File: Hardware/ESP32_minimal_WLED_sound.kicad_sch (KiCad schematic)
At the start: 42 parts, among them J1 Conn_01x04_Male, J2 USB_C_Receptacle_USB2.0, J3 Conn_01x02_Male, Q1 AO3400A, SW1 Reset, SW2 Boot, U1 LM1117-3.3, U2 ESP32-S2-WROVER, U3 USBLC6-2SC6, U4 TXS0102DCT

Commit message: update to V1
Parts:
- removed C3, C4: 20p, Capacitor_SMD:C_0603_1608Metric, symbol Device:C_Small
- removed C5, C9: 0.1u, Capacitor_SMD:C_0603_1608Metric, symbol Device:C_Small
- removed D1: LED, LED_SMD:LED_0603_1608Metric, symbol Device:LED_Small
- removed FB1, FB2: >1A, Inductor_SMD:L_0603_1608Metric, symbol Device:Ferrite_Bead_Small
- removed JP1: SolderJumper_2_Bridged, Jumper:SolderJumper-2_P1.3mm_Bridged_RoundedPad1.0x1.5mm, symbol Jumper:SolderJumper_2_Bridged
- removed JP2: SolderJumper_3_Bridged12, Jumper:SolderJumper-3_P1.3mm_Bridged12_Pad1.0x1.5mm, symbol Jumper:SolderJumper_3_Bridged12
- removed R2: 100r, Resistor_SMD:R_0603_1608Metric, symbol Device:R_Small
- removed R3, R4: 22r, Resistor_SMD:R_0603_1608Metric, symbol Device:R_Small
- removed SW1: Reset, ESP32-S2-Breakout:Alps_SKRK, symbol Switch:SW_Push
- removed U2: ESP32-S2-WROVER, RF_Module:ESP32-S2-WROVER, symbol RF_Module:ESP32-S2-WROVER
- removed U3: USBLC6-2SC6, Package_TO_SOT_SMD:SOT-23-6, symbol Power_Protection:USBLC6-2SC6
- added C3, C4, C9: 0.1uF, Capacitor_SMD:C_0805_2012Metric, symbol Device:C
- added C5: 0.1uF, Capacitor_SMD:C_0603_1608Metric, symbol Device:C
- added J4: Barrel_Jack_Switch_Pin3Ring, Connector_BarrelJack:BarrelJack_GCT_DCJ200-10-A_Horizontal, symbol Connector:Barrel_Jack_Switch_Pin3Ring
- added J5, J6: Conn_01x03_Male, Connector_JST:JST_EH_B3B-EH-A_1x03_P2.50mm_Vertical, symbol Connector:Conn_01x03_Male
- added J7, J9: Conn_01x03_Male, Connector_PinHeader_2.54mm:PinHeader_1x03_P2.54mm_Vertical, symbol Connector:Conn_01x03_Male
- added J8: Conn_01x02_Male, TerminalBlock_Phoenix:TerminalBlock_Phoenix_MKDS-1,5-2-5.08_1x02_P5.08mm_Horizontal, symbol Connector:Conn_01x02_Male
- added JP1: SolderJumper_3_Open, Jumper:SolderJumper-3_P1.3mm_Open_Pad1.0x1.5mm, symbol Jumper:SolderJumper_3_Open
- added MK1: ICS-43434, ICS-43434:MIC_ICS-43434, symbol ICS-43434:ICS-43434
- added R14, R15: 4,7k, Resistor_SMD:R_0603_1608Metric, symbol Device:R
- added R2: 0.01, Resistor_SMD:R_0805_2012Metric, symbol Device:R
- added R3, R4: 10, Resistor_SMD:R_0603_1608Metric, symbol Device:R
- added U2: INA226, Package_SO:VSSOP-10_3x3mm_P0.5mm, symbol Analog_ADC:INA226
- added U3: LM1117-3.3, Package_TO_SOT_SMD:SOT-223, symbol Regulator_Linear:LM1117-3.3
- added U5: ESP32-WROOM-32, RF_Module:ESP32-WROOM-32, symbol RF_Module:ESP32-WROOM-32
- C10, C11: footprint Capacitor_SMD:C_0603_1608Metric_Pad1.08x0.95mm_HandSolder -> Capacitor_SMD:C_0603_1608Metric
- J1: footprint Connector_PinHeader_2.54mm:PinHeader_1x04_P2.54mm_Horizontal -> Connector_PinHeader_2.54mm:PinHeader_1x04_P2.54mm_Vertical
- J2: footprint ESP32-S2-Breakout:USB_C_Receptacle_HRO_TYPE-C-31-M-12 -> Connector_USB:USB_C_Receptacle_HRO_TYPE-C-31-M-12
- J3: footprint Connector_Phoenix_MSTB:PhoenixContact_MSTBA_2,5_2-G-5,08_1x02_P5.08mm_Horizontal -> TerminalBlock_Phoenix:TerminalBlock_Phoenix_MKDS-1,5-2-5.08_1x02_P5.08mm_Horizontal
- R1: value 10k -> 1M; LCSC C99198 -> C163928
- R12, R13: footprint Capacitor_SMD:C_0603_1608Metric_Pad1.08x0.95mm_HandSolder -> Resistor_SMD:R_0603_1608Metric
- R6, R7, R9: footprint Resistor_SMD:R_0805_2012Metric -> Resistor_SMD:R_0603_1608Metric
- R8: value 100r -> 100
- SW2: footprint ESP32-S2-Breakout:Alps_SKRK -> Button_Switch_SMD:SW_SPST_B3U-1000P-B
- U1: value LM1117-3.3 -> LM1117-5
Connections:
- net VBUS is gone; now on net +5V: J2.A4 (VBUS), J2.A9 (VBUS), J2.B4 (VBUS), J2.B9 (VBUS)
- net +12V: now also C5.2, J4.1, J8.1 (Pin_1), R2.2, R3.1; no longer J1.4 (Pin_4)
- net +3V3: now also J1.4 (Pin_4), R8.1, C4.2, C9.1, MK1.5 (VDD), R14.2, R15.1, U2.6 (VS), U3.2 (VO), U5.2 (VDD); no longer C2.2, J1.3 (Pin_3), R1.1, U1.2 (VO)
- net +5V: now also C2.2, U1.2 (VO), C3.1, J5.1 (Pin_1), J6.1 (Pin_1), J7.1 (Pin_1), J9.1 (Pin_1), JP1.1 (A), U3.3 (VI); no longer C1.1, U1.3 (VI)
- net EN: now also C7.2, U5.3 (EN)
- net GND: now also R1.2, C3.2, C4.1, C9.2, J4.2, J4.3, J5.3 (Pin_3), J6.3 (Pin_3), J7.3 (Pin_3), J8.2 (Pin_2), J9.3 (Pin_3), MK1.2 (LR), MK1.3 (GND), U2.1 (A1), U2.2 (A0), U2.7 (GND), U3.1 (GND), U5.1 (GND), U5.15 (GND), U5.38 (GND), U5.39 (GND); no longer C7.2
- net IO00: now also U5.25 (IO0)
- net O1V: now also JP1.2 (C)
- net U_GND: now reaches C8.2, J2.S1 (SHIELD)
- net U_GND: now also R1.1
- net +5VD: no longer names the net of J1.2 (Pin_2)
- net +5VD: now also U5.34 (RXD0/IO3)
- net GPIO_0 renamed GPIO_2
- net GPIO_2: now also U5.24 (IO2); no longer U4.4 (A2)
- net WS2812B_GPIO_0 renamed WS2812B_2
- net WS2812B_2: now also J5.2 (Pin_2), J7.2 (Pin_2); no longer R13.2
- new net: R4.1, U2.9 (Vin-)
- new net: J1.3 (Pin_3), U5.35 (TXD0/IO1)
- new net: R3.2, U2.10 (Vin+)
- new net +12VA: C1.1, C5.1, JP1.3 (B), R2.1, R4.2, U1.3 (VI)
- new net GPIO_4: U4.4 (A2), U5.26 (IO4)
- new net SCK: MK1.4 (SCK), R15.2, U2.5 (SCL), U5.13 (IO14)
- new net SD: MK1.6 (SD), R14.1, U2.4 (SDA), U5.8 (IO32)
- new net WS: MK1.1 (WS), U5.23 (IO15)
- new net WS2812B_4: J6.2 (Pin_2), J9.2 (Pin_2), R13.2
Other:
- note added: "12V to 5V"
- note added: "Connector"
- note added: "ESP32"
- note added: "INA Current sensor"
- note added: "MIC"
- note removed: "USB Connector & ESD"
- moved on the sheet: C6, C7, C8, D2, D3, D4, J2, J3, Q1, R10, R11, R5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

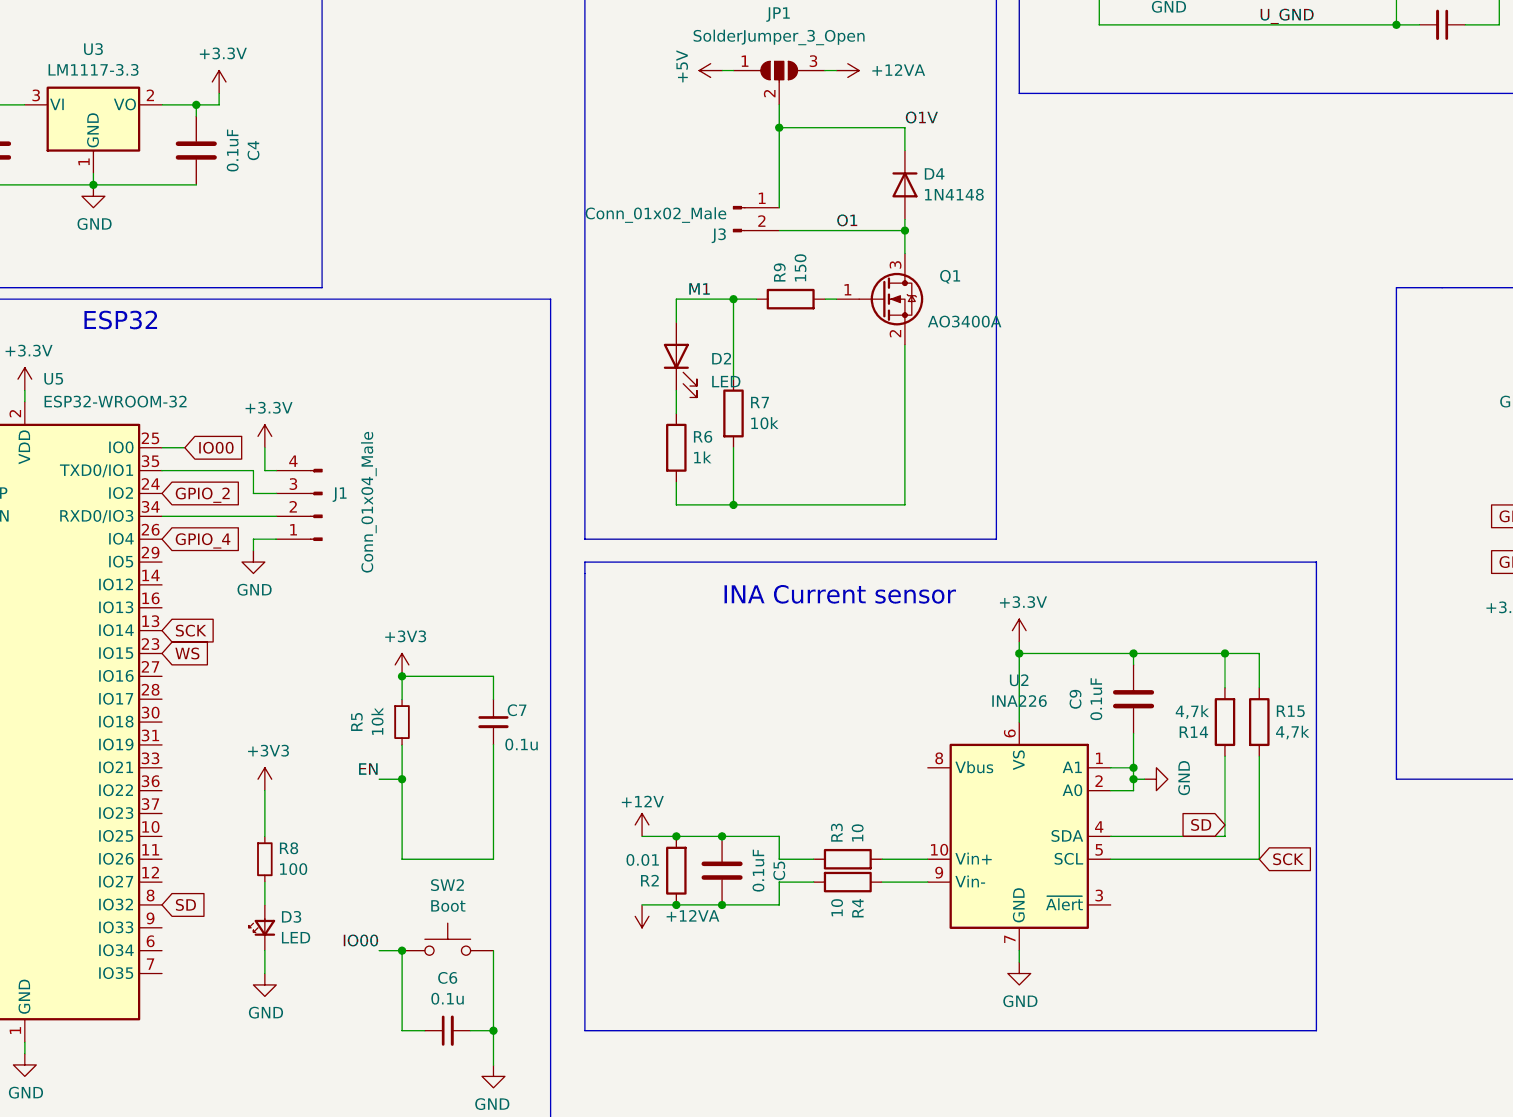
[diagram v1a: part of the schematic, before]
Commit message: fix esp32 EN and IO0, Todo: solder jumper and 12V to 5V
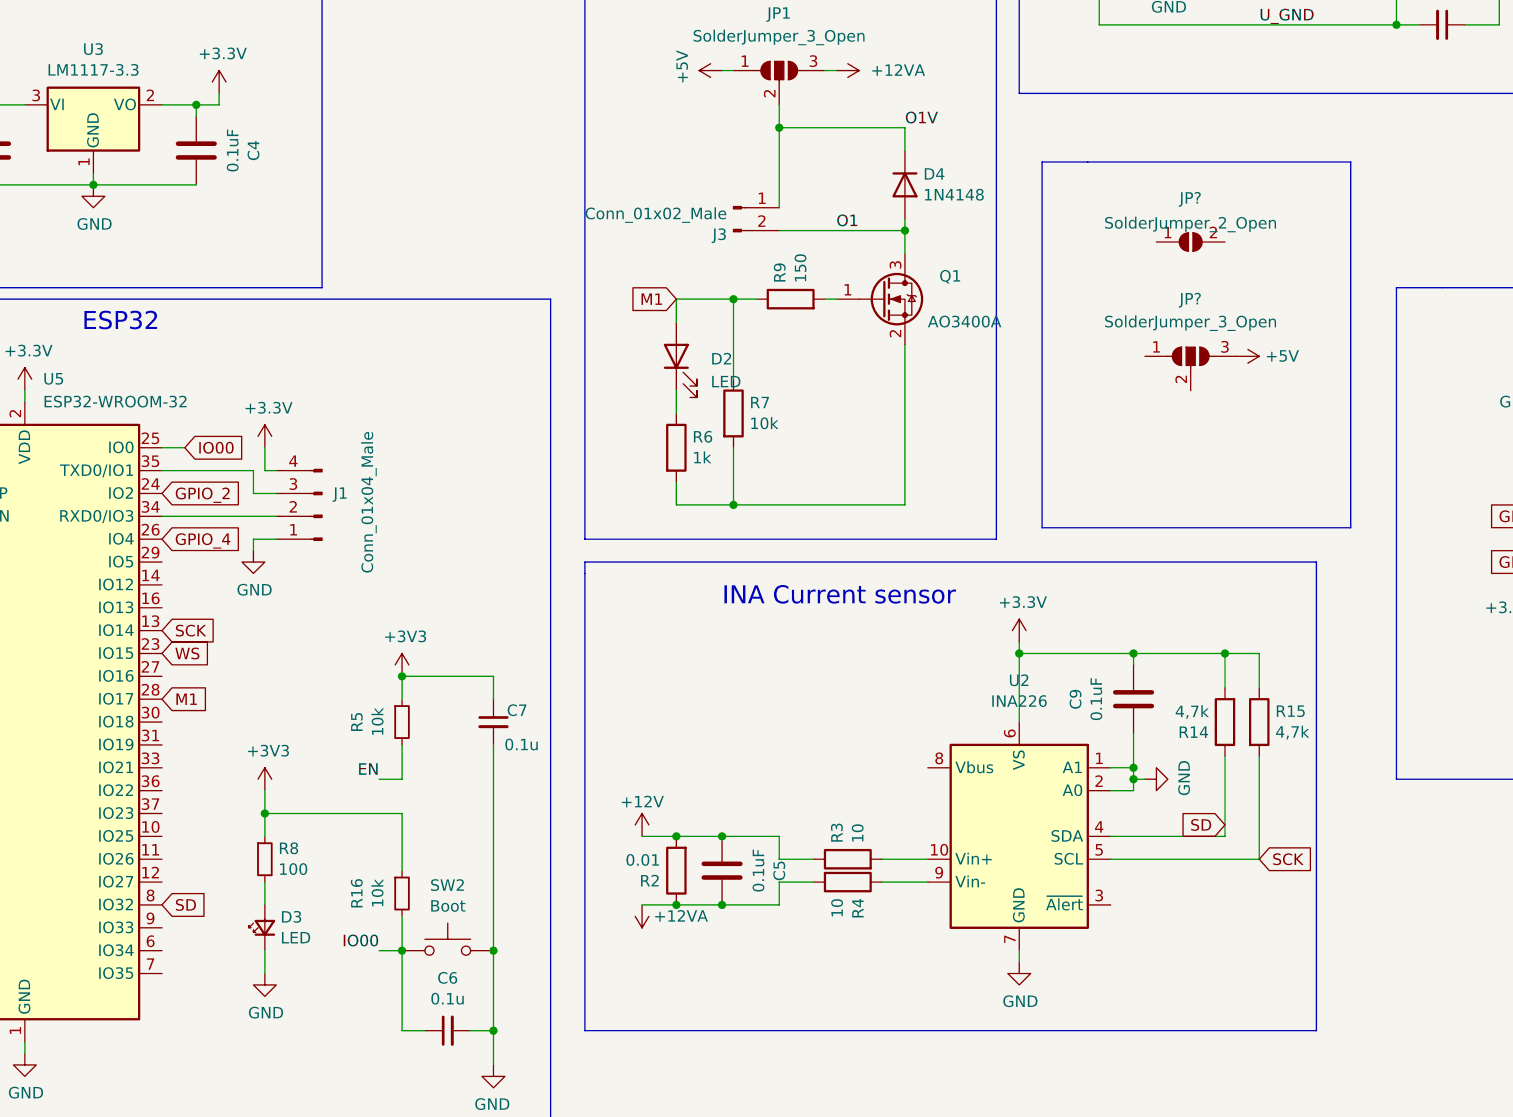
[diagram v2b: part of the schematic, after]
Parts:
- added JP?: SolderJumper_3_Open, Jumper:SolderJumper-3_P1.3mm_Open_Pad1.0x1.5mm, symbol Jumper:SolderJumper_3_Open
- added JP?: SolderJumper_2_Open, Jumper:SolderJumper-2_P1.3mm_Open_Pad1.0x1.5mm, symbol Jumper:SolderJumper_2_Open
- added R16: 10k, Resistor_SMD:R_0603_1608Metric, symbol Device:R_Small
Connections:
- net +3V3: now also R16.1
- net +5V: now also JP?.3 (B)
- net EN: no longer C7.2
- net GND: now also C7.2
- net IO00: now also R16.2
- net M1: now also U5.28 (IO17)
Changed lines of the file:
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@@
   (junction (at 207.01 66.04) (diameter 0) (color 0 0 0 0)
   )
+  (junction (at 95.25 173.99) (diameter 0) (color 0 0 0 0)
+  )
   (junction (at 95.25 182.88) (diameter 0) (color 0 0 0 0)
   )
@@
   (junction (at 50.8 45.72) (diameter 0) (color 0 0 0 0)
   )
+  (junction (at 69.85 158.75) (diameter 0) (color 0 0 0 0)
+  )
   (junction (at 50.8 88.9) (diameter 0) (color 0 0 0 0)
   )
@@
   )
   (junction (at 224.79 113.03) (diameter 0) (color 0 0 0 0)
-  )
-  (junction (at 85.09 154.94) (diameter 0) (color 0 0 0 0)
   )
   (junction (at 115.57 161.29) (diameter 0) (color 0 0 0 0)
@@
     (stroke (width 0) (type default) (color 0 0 0 0))
   )
+  (wire (pts (xy 85.09 158.75) (xy 69.85 158.75))
+    (stroke (width 0) (type default) (color 0 0 0 0))
+  )
   (wire (pts (xy 264.16 66.04) (xy 264.16 64.77))
     (stroke (width 0) (type default) (color 0 0 0 0))
@@
     (stroke (width 0) (type default) (color 0 0 0 0))
   )
-  (wire (pts (xy 69.85 156.21) (xy 69.85 161.29))
+  (wire (pts (xy 69.85 156.21) (xy 69.85 158.75))
     (stroke (width 0) (type default) (color 0 0 0 0))
   )
@@
     (stroke (width 0) (type default) (color 0 0 0 0))
   )
-  (wire (pts (xy 95.25 151.13) (xy 95.25 163.83))
+  (wire (pts (xy 95.25 151.13) (xy 95.25 173.99))
     (stroke (width 0) (type default) (color 0 0 0 0))
   )
@@
     (stroke (width 0) (type default) (color 0 0 0 0))
   )
+  (wire (pts (xy 85.09 170.18) (xy 85.09 173.99))
+    (stroke (width 0) (type default) (color 0 0 0 0))
+  )
   (wire (pts (xy 196.85 26.67) (xy 196.85 24.13))
     (stroke (width 0) (type default) (color 0 0 0 0))
@@
     (stroke (width 0) (type default) (color 0 0 0 0))
   )
-  (wire (pts (xy 85.09 163.83) (xy 95.25 163.83))
-    (stroke (width 0) (type default) (color 0 0 0 0))
-  )
   (wire (pts (xy 140.97 93.98) (xy 140.97 92.71))
     (stroke (width 0) (type default) (color 0 0 0 0))
@@
     (stroke (width 0) (type default) (color 0 0 0 0))
   )
+  (wire (pts (xy 85.09 165.1) (xy 85.09 158.75))
+    (stroke (width 0) (type default) (color 0 0 0 0))
+  )
   (wire (pts (xy 195.58 60.96) (xy 198.12 60.96))
     (stroke (width 0) (type default) (color 0 0 0 0))
@@
     (stroke (width 0) (type default) (color 0 0 0 0))
   )
+  (polyline (pts (xy 156.21 86.36) (xy 161.29 86.36))
+    (stroke (width 0) (type default) (color 0 0 0 0))
+  )
+  (polyline (pts (xy 190.5 86.36) (xy 190.5 127))
+    (stroke (width 0) (type default) (color 0 0 0 0))
+  )
   (wire (pts (xy 166.37 140.97) (xy 153.67 140.97))
     (stroke (width 0) (type default) (color 0 0 0 0))
@@
     (stroke (width 0) (type default) (color 0 0 0 0))
   )
+  (polyline (pts (xy 156.21 127) (xy 156.21 86.36))
+    (stroke (width 0) (type default) (color 0 0 0 0))
+  )
   (wire (pts (xy 265.43 53.34) (xy 265.43 52.07))
     (stroke (width 0) (type default) (color 0 0 0 0))
@@
     (stroke (width 0) (type default) (color 0 0 0 0))
   )
-  (wire (pts (xy 85.09 154.94) (xy 85.09 163.83))
-    (stroke (width 0) (type default) (color 0 0 0 0))
-  )
   (polyline (pts (xy 151.13 128.27) (xy 151.13 63.5))
     (stroke (width 0) (type default) (color 0 0 0 0))
@@
     (stroke (width 0) (type default) (color 0 0 0 0))
   )
+  (polyline (pts (xy 190.5 127) (xy 156.21 127))
+    (stroke (width 0) (type default) (color 0 0 0 0))
+  )
   (wire (pts (xy 127 166.37) (xy 127 168.91))
     (stroke (width 0) (type default) (color 0 0 0 0))
@@
     (stroke (width 0) (type default) (color 0 0 0 0))
   )
+  (polyline (pts (xy 161.29 86.36) (xy 190.5 86.36))
+    (stroke (width 0) (type default) (color 0 0 0 0))
+  )
   (polyline (pts (xy 105.41 132.08) (xy 105.41 182.88))
     (stroke (width 0) (type default) (color 0 0 0 0))
@@
   )
   (wire (pts (xy 36.83 36.83) (xy 39.37 36.83))
+    (stroke (width 0) (type default) (color 0 0 0 0))
+  )
+  (wire (pts (xy 69.85 158.75) (xy 69.85 161.29))
     (stroke (width 0) (type default) (color 0 0 0 0))
   )
@@
   )
   (label "O1" (at 133.35 93.98 0)
-    (effects (font (size 1.27 1.27)) (justify left bottom))
-  )
-  (label "M1" (at 116.84 101.6 0)
     (effects (font (size 1.27 1.27)) (justify left bottom))
   )
@@
     )
   )
+  (global_label "M1" (shape input) (at 115.57 101.6 180) (fields_autoplaced)
+    (effects (font (size 1.27 1.27)) (justify right))
+    (property "Intersheet References" "${INTERSHEET_REFS}" (id 0) (at 110.4959 101.5206 0)
+      (effects (font (size 1.27 1.27)) (justify right) hide)
+    )
+  )
   (global_label "SD" (shape input) (at 104.14 44.45 180) (fields_autoplaced)
     (effects (font (size 1.27 1.27)) (justify right))
@@
     (effects (font (size 1.27 1.27)) (justify left))
     (property "Intersheet References" "${INTERSHEET_REFS}" (id 0) (at 63.4941 141.0494 0)
+      (effects (font (size 1.27 1.27)) (justify left) hide)
+    )
+  )
+  (global_label "M1" (shape input) (at 58.42 146.05 0) (fields_autoplaced)
+    (effects (font (size 1.27 1.27)) (justify left))
+    (property "Intersheet References" "${INTERSHEET_REFS}" (id 0) (at 63.4941 145.9706 0)
       (effects (font (size 1.27 1.27)) (justify left) hide)
     )
@@
     (pin "2")
   )
+  (symbol (lib_id "Jumper:SolderJumper_3_Open") (at 172.72 107.95 0) (unit 1)
+    (in_bom yes) (on_board yes) (fields_autoplaced)
+    (property "Reference" "JP?" (id 0) (at 172.72 101.6 0))
+    (property "Value" "SolderJumper_3_Open" (id 1) (at 172.72 104.14 0))
+    (property "Footprint" "Jumper:SolderJumper-3_P1.3mm_Open_Pad1.0x1.5mm" (id 2) (at 172.72 107.95 0)
+      (effects (font (size 1.27 1.27)) hide)
+    )
+    (property "Datasheet" "~" (id 3) (at 172.72 107.95 0)
+      (effects (font (size 1.27 1.27)) hide)
+    )
+    (pin "1")
+    (pin "2")
+    (pin "3")
+  )
   (symbol (lib_id "Jumper:SolderJumper_3_Open") (at 127 76.2 0) (unit 1)
     (in_bom yes) (on_board yes) (fields_autoplaced)
@@
     (pin "1")
   )
+  (symbol (lib_id "power:+5V") (at 177.8 107.95 270) (unit 1)
+    (in_bom yes) (on_board yes)
+    (property "Reference" "#PWR0149" (id 0) (at 173.99 107.95 0)
+      (effects (font (size 1.27 1.27)) hide)
+    )
+    (property "Value" "+5V" (id 1) (at 182.88 107.95 90))
+    (property "Footprint" "" (id 2) (at 177.8 107.95 0)
+      (effects (font (size 1.27 1.27)) hide)
+    )
+    (property "Datasheet" "" (id 3) (at 177.8 107.95 0)
+      (effects (font (size 1.27 1.27)) hide)
+    )
+    (pin "1")
+  )
+  (symbol (lib_id "Device:R_Small") (at 85.09 167.64 0) (unit 1)
+    (in_bom yes) (on_board yes)
+    (property "Reference" "R16" (id 0) (at 80.1116 167.64 90))
+    (property "Value" "10k" (id 1) (at 82.423 167.64 90))
+    (property "Footprint" "Resistor_SMD:R_0603_1608Metric" (id 2) (at 85.09 167.64 0)
+      (effects (font (size 1.27 1.27)) hide)
+    )
+    (property "Datasheet" "~" (id 3) (at 85.09 167.64 0)
+      (effects (font (size 1.27 1.27)) hide)
+    )
+    (property "LCSC" "C99198" (id 4) (at 85.09 167.64 90)
+      (effects (font (size 1.27 1.27)) hide)
+    )
+    (pin "1")
+    (pin "2")
+  )
   (symbol (lib_id "power:+3.3V") (at 214.63 135.89 90) (unit 1)
     (in_bom yes) (on_board yes) (fields_autoplaced)
@@
     (pin "1")
   )
+  (symbol (lib_id "Jumper:SolderJumper_2_Open") (at 172.72 95.25 0) (unit 1)
+    (in_bom yes) (on_board yes) (fields_autoplaced)
+    (property "Reference" "JP?" (id 0) (at 172.72 90.3945 0))
+    (property "Value" "SolderJumper_2_Open" (id 1) (at 172.72 93.1696 0))
+    (property "Footprint" "Jumper:SolderJumper-2_P1.3mm_Open_Pad1.0x1.5mm" (id 2) (at 172.72 95.25 0)
+      (effects (font (size 1.27 1.27)) hide)
+    )
+    (property "Datasheet" "~" (id 3) (at 172.72 95.25 0)
+      (effects (font (size 1.27 1.27)) hide)
+    )
+    (pin "1")
+    (pin "2")
+  )
   (symbol (lib_id "power:+5V") (at 241.3 59.69 270) (unit 1)
     (in_bom yes) (on_board yes)
@@
   )
   (symbol (lib_id "power:+12VA") (at 111.76 168.91 180) (unit 1)
-    (in_bom yes) (on_board yes) (fields_autoplaced)
+    (in_bom yes) (on_board yes)
     (property "Reference" "#PWR0145" (id 0) (at 111.76 165.1 0)
       (effects (font (size 1.27 1.27)) hide)
     )
-    (property "Value" "+12VA" (id 1) (at 114.3 170.1799 0)
+    (property "Value" "+12VA" (id 1) (at 113.03 170.18 0)
       (effects (font (size 1.27 1.27)) (justify right))
     )
@@
       (reference "#PWR0147") (unit 1) (value "+12VA") (footprint "")
     )
+    (path "/8529ad27-a755-4c72-a97c-9956a64bac23"
+      (reference "#PWR0149") (unit 1) (value "+5V") (footprint "")
+    )
     (path "/71fcaf2d-3d18-47e2-98e4-fd8aef739eff"
       (reference "C1") (unit 1) (value "0.1uF") (footprint "Capacitor_SMD:C_0805_2012Metric")
@@
       (reference "JP1") (unit 1) (value "SolderJumper_3_Open") (footprint "Jumper:SolderJumper-3_P1.3mm_Open_Pad1.0x1.5mm")
     )
+    (path "/258a04da-e0e4-47a9-8cae-c371fe7384dc"
+      (reference "JP?") (unit 1) (value "SolderJumper_3_Open") (footprint "Jumper:SolderJumper-3_P1.3mm_Open_Pad1.0x1.5mm")
+    )
+    (path "/a3f59d24-7246-4797-9eb0-3fcb8deb27ae"
+      (reference "JP?") (unit 1) (value "SolderJumper_2_Open") (footprint "Jumper:SolderJumper-2_P1.3mm_Open_Pad1.0x1.5mm")
+    )
     (path "/f836980c-656c-43a3-bc29-955cf8b0213a"
       (reference "MK1") (unit 1) (value "ICS-43434") (footprint "ICS-43434:MIC_ICS-43434")
@@
       (reference "R15") (unit 1) (value "4,7k") (footprint "Resistor_SMD:R_0603_1608Metric")
     )
+    (path "/8656927c-d21a-4c21-bbce-59fe9fc6c17c"
+      (reference "R16") (unit 1) (value "10k") (footprint "Resistor_SMD:R_0603_1608Metric")
+    )
     (path "/187e6a3d-15f8-48d4-b349-faeea074addb"
